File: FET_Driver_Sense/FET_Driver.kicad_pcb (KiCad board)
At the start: 2 copper layers, 32 x 25 mm, 16 parts, among them J101 Interface, J102 Out, Q101 IRF5210SPbF, U101 EL3H7(C)(TA)-G, U102 ACS712xLCTR-20A, U603 H7550-H#

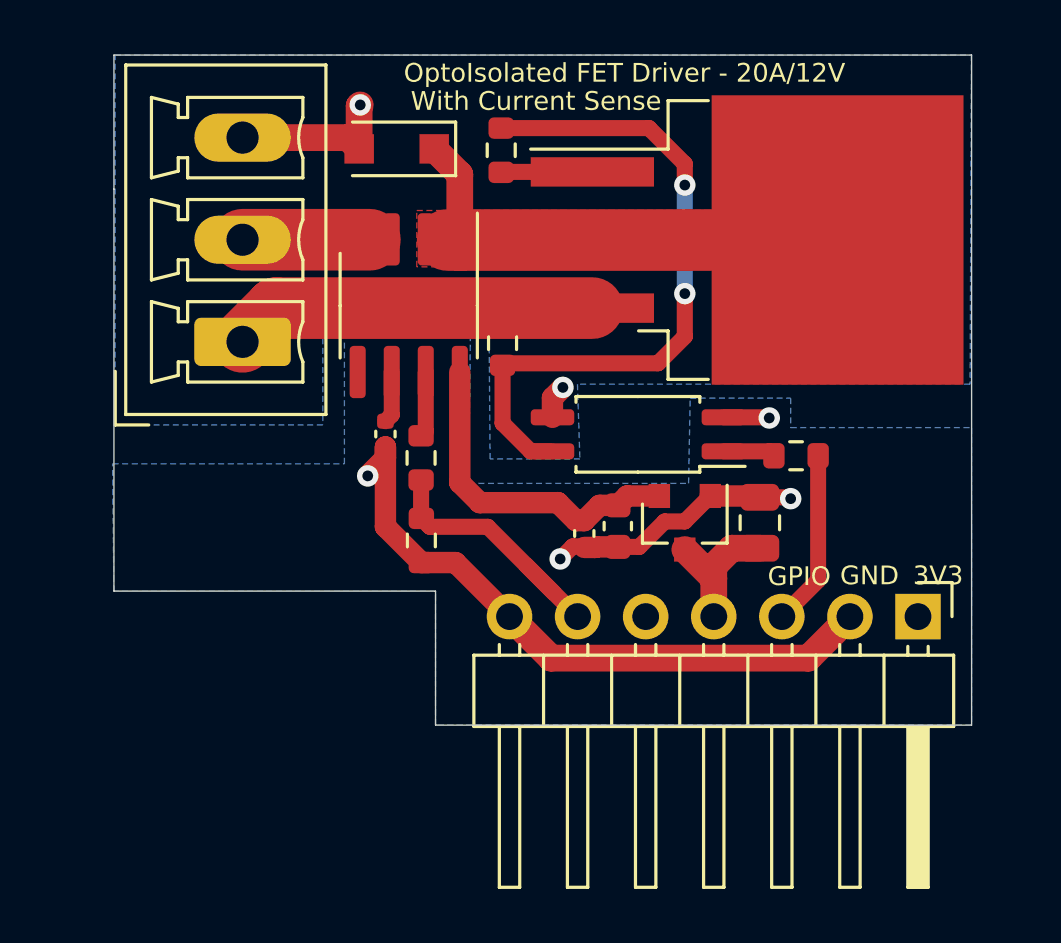
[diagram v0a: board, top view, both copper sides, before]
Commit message: Opto Tacho (Schmidtt),   Fixes to FET_Driver_Sense
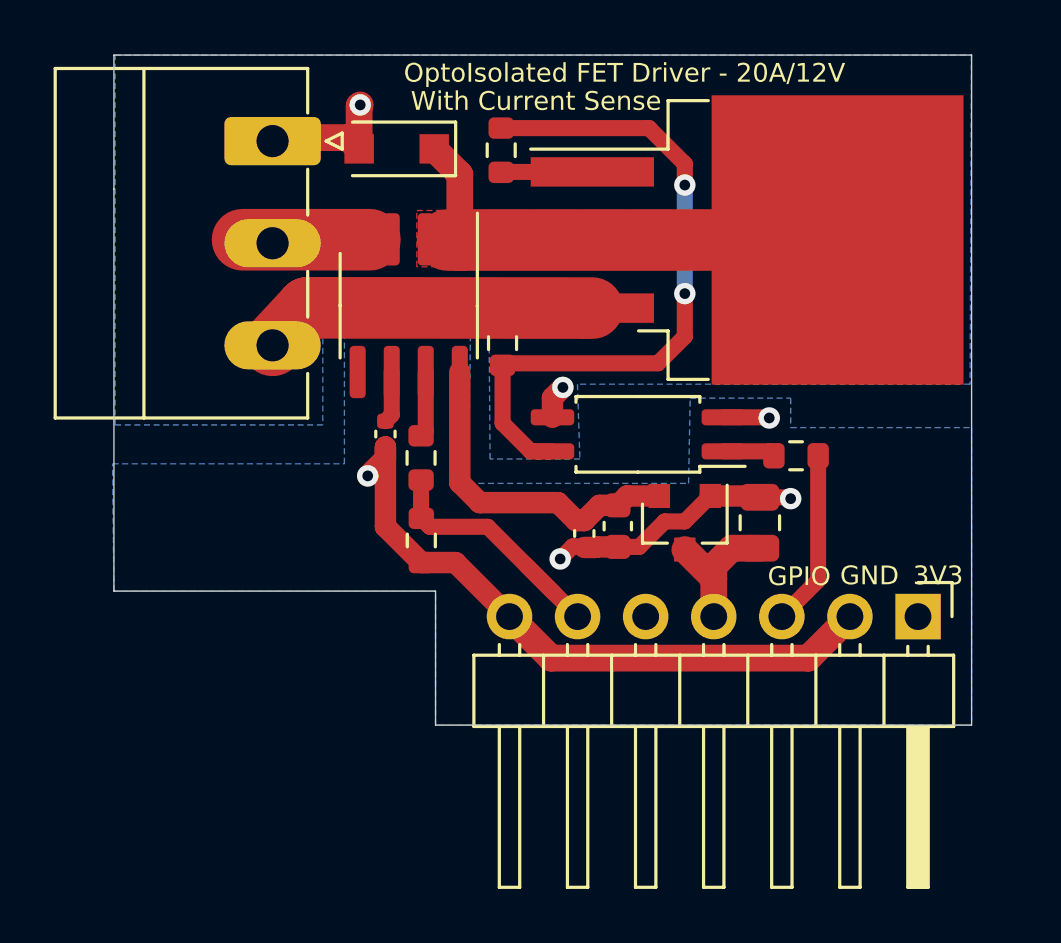
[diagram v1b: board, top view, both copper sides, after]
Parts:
- J102: footprint Connector_Phoenix_MC:PhoenixContact_MCV_1,5_3-G-3.81_1x03_P3.81mm_Vertical -> Connector_Phoenix_MC:PhoenixContact_MC_1,5_3-G-3.81_1x03_P3.81mm_Horizontal
- moved J102 7.57 mm to (113.9, 71.2), turned to 270 degrees
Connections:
- J102 pad 1: /ISO_VIN -> /ISO_GND
- J102 pad 3: /ISO_GND -> /ISO_VIN
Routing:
- net /ISO_VIN: track 17.1 -> 16.1 mm

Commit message: FET Driver - LCSC Parts tidy up
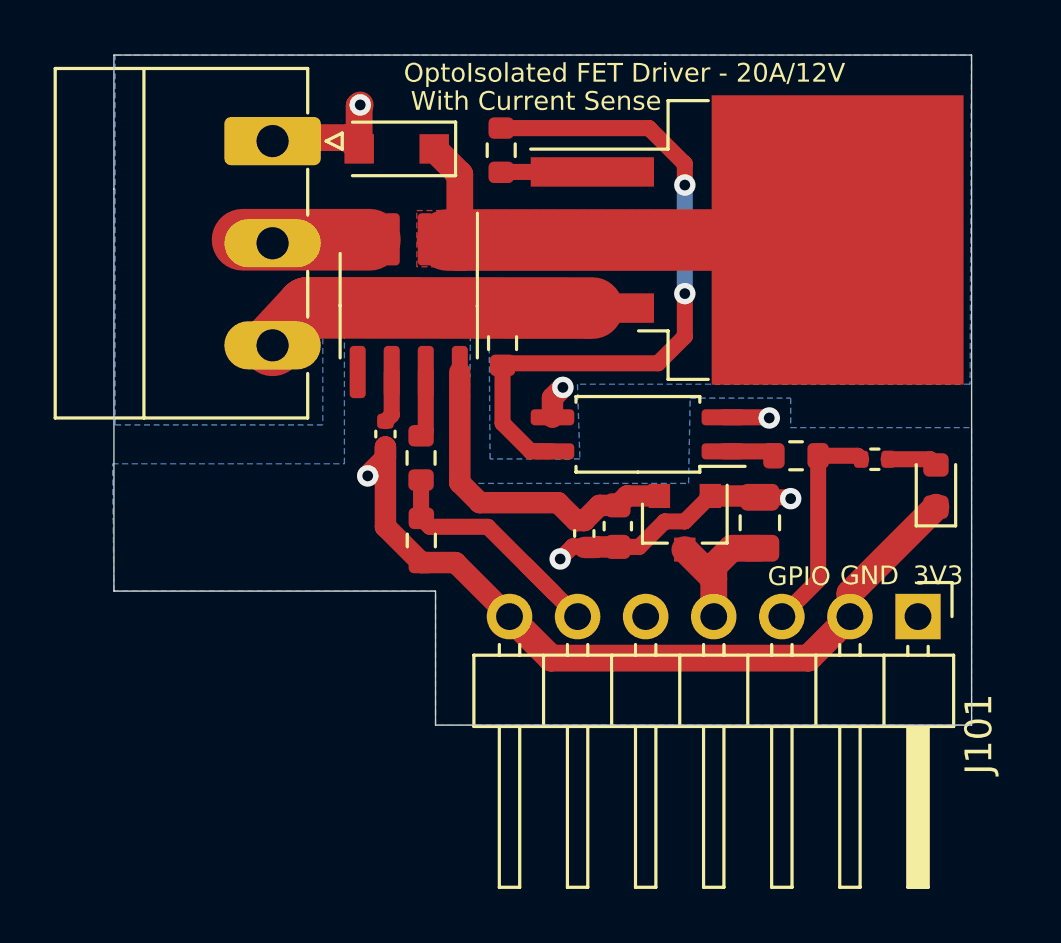
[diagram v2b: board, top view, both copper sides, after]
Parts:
- added D102: GREEN LED, LED_SMD:LED_0603_1608Metric, F.Cu at (138.7, 84.1)
- added R105: 2k, Resistor_SMD:R_0402_1005Metric, F.Cu at (136.4, 83.1)
- Q101: value IRF5210SPbF -> IRF5210STRLPBF
- U102: value ACS712xLCTR-20A -> ACS712ELCTR-20A-T
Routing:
- net GND: track 35.7 -> 41.1 mm
- net Net-(D102-Pad2): track 0.00 -> 1.86 mm
- net /GPIO: track 7.01 -> 8.67 mm
